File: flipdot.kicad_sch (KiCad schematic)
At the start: 48 parts, among them J1 Conn_01x02_Pin, J2 Conn_01x02_Pin, J3 Conn_01x02_Pin, J4 Conn_01x12_Pin, U5 74HC595

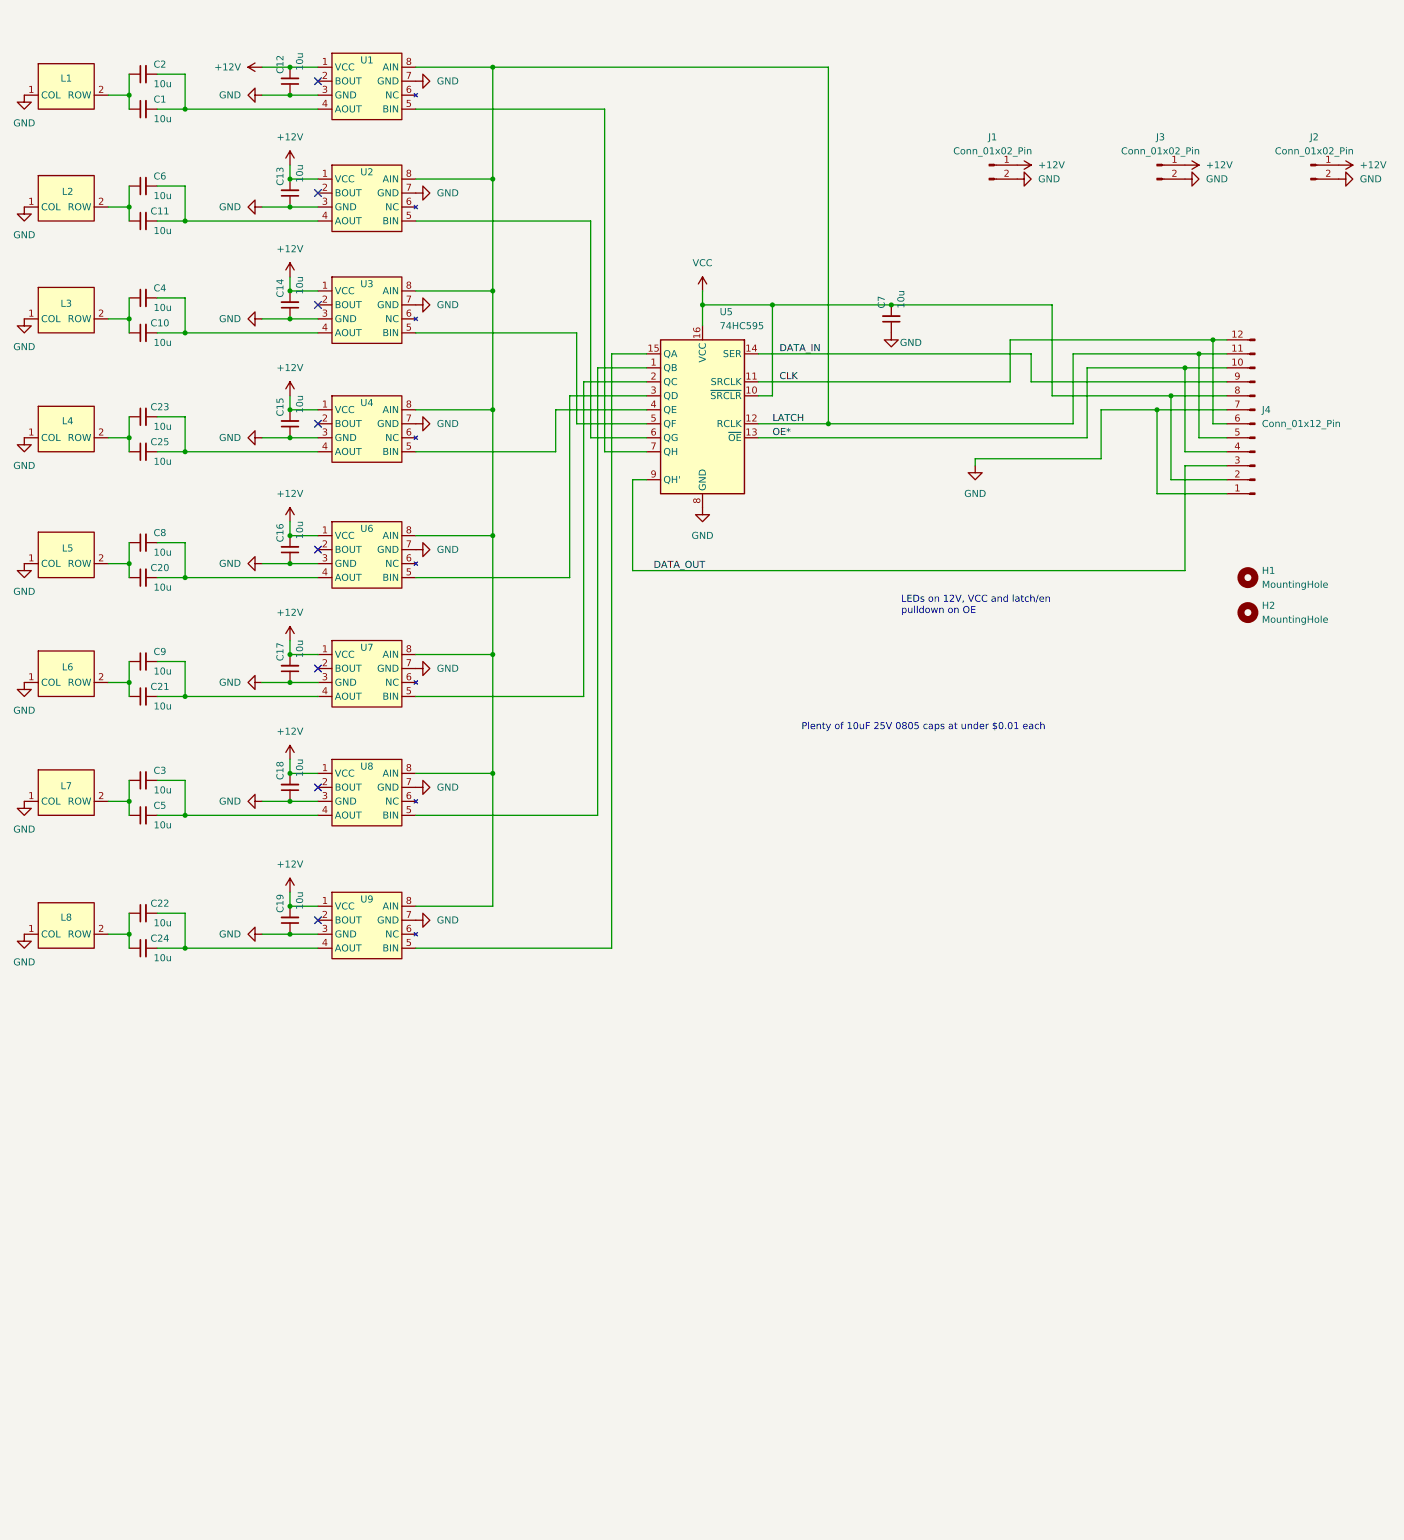
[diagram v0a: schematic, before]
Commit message: split into separate sheets
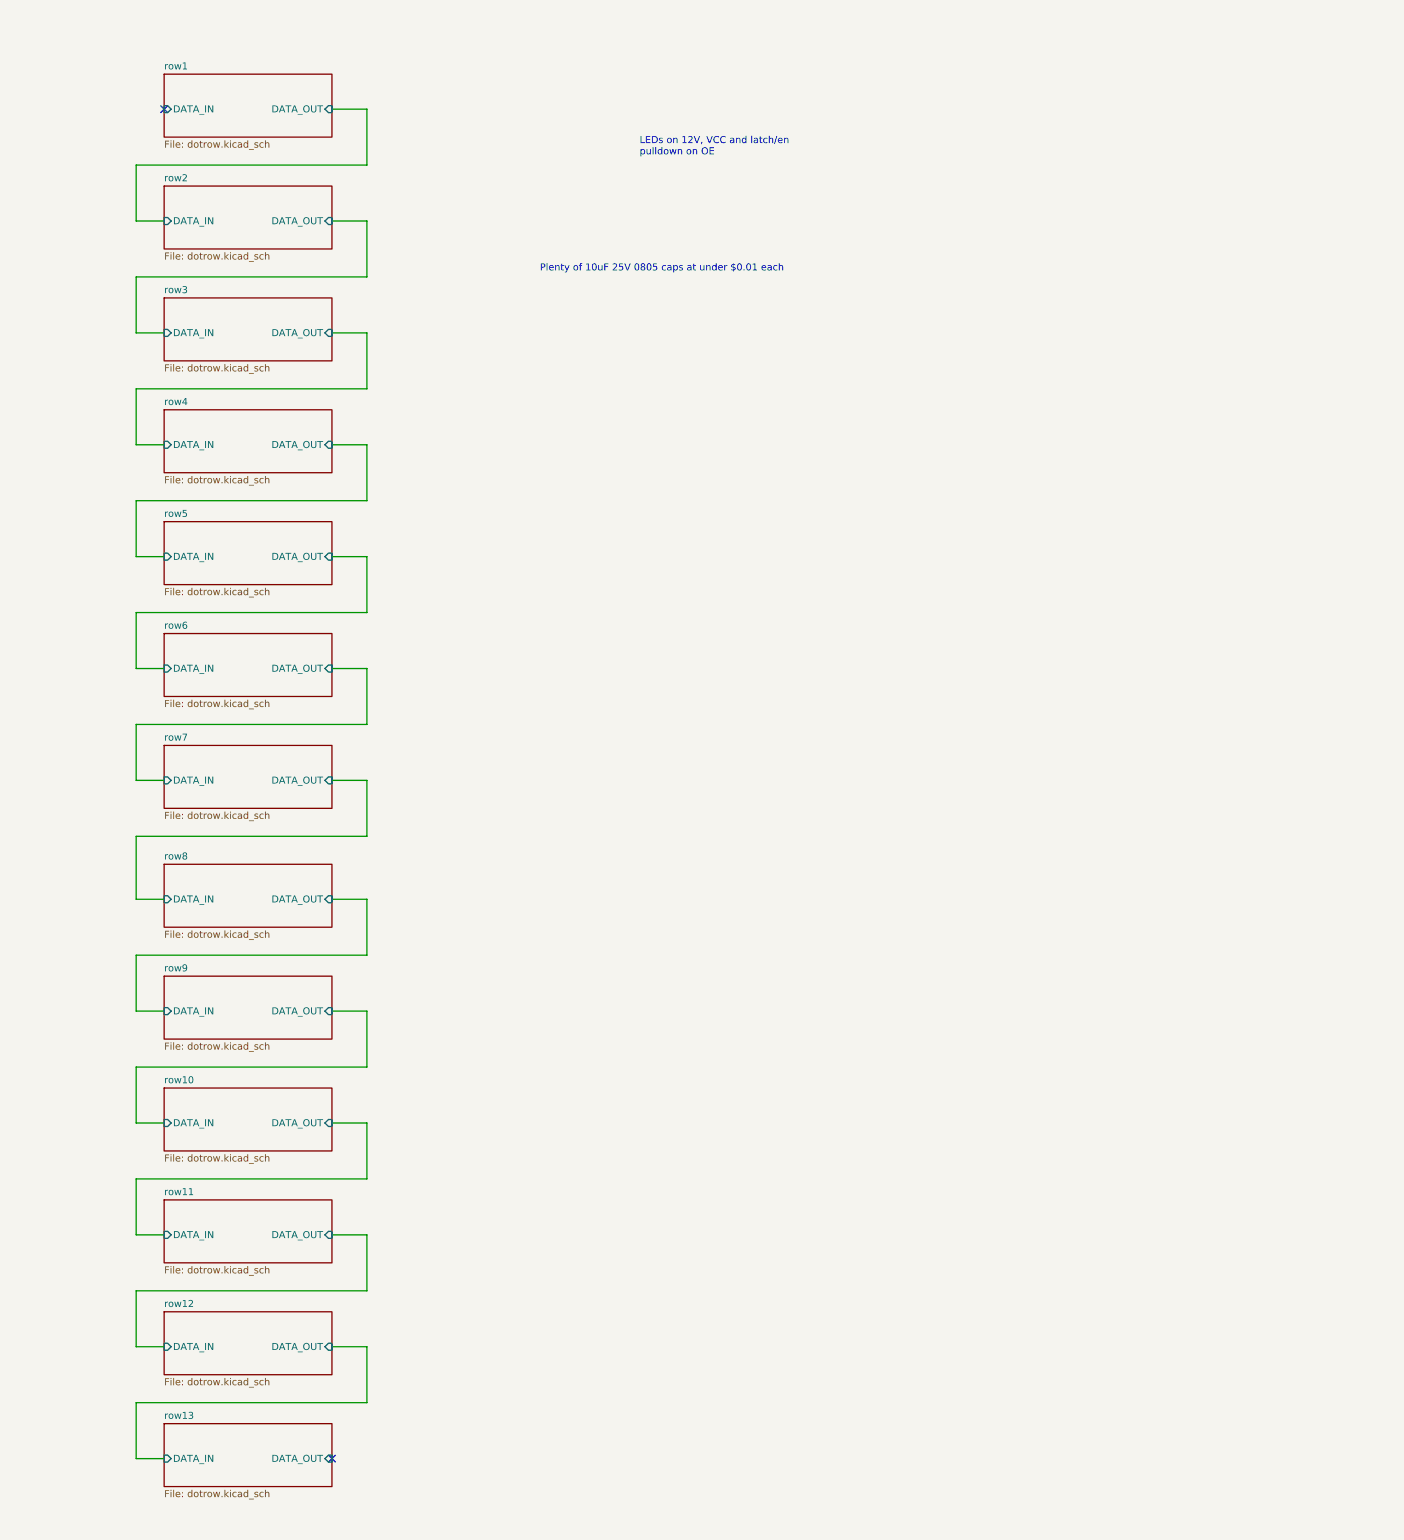
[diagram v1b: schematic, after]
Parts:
- removed C1, C10, C11, C12, C13, C14, C15, C16, C17, C18, C19, C2, C20, C21, C22, C23, C24, C25, C3, C4, C5, C6, C7, C8, C9: 10u, Capacitor_SMD:C_0805_2012Metric, symbol Device:C_Small
- removed H1, H2: MountingHole, MountingHole:MountingHole_3.2mm_M3_DIN965, symbol Mechanical:MountingHole
- removed J1, J2, J3: Conn_01x02_Pin, Connector_JST:JST_VH_B2P-VH_1x02_P3.96mm_Vertical, symbol Connector:Conn_01x02_Pin
- removed J4: Conn_01x12_Pin, Connector_JST:JST_ZH_B6B-ZR_1x06_P1.50mm_Vertical, symbol Connector:Conn_01x12_Pin
- removed L1, L2, L3, L4, L5, L6, L7, L8: ~, Flipdot:Flipdot_single, symbol Flipdot:flipdot_single
- removed U1, U2, U3, U4, U6, U7, U8, U9: ~, Package_SO:SOP-8_3.9x4.9mm_P1.27mm, symbol Flipdot:MX6208
- removed U5: 74HC595, Package_SO:SOP-16_3.9x9.9mm_P1.27mm, symbol 74xx:74HC595
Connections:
- no-connect marks 8 -> 2
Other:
- added sheet row1 (dotrow.kicad_sch)
- added sheet row10 (dotrow.kicad_sch)
- added sheet row11 (dotrow.kicad_sch)
- added sheet row12 (dotrow.kicad_sch)
- added sheet row13 (dotrow.kicad_sch)
- added sheet row2 (dotrow.kicad_sch)
- added sheet row3 (dotrow.kicad_sch)
- added sheet row4 (dotrow.kicad_sch)
- added sheet row5 (dotrow.kicad_sch)
- added sheet row6 (dotrow.kicad_sch)
- added sheet row7 (dotrow.kicad_sch)
- added sheet row8 (dotrow.kicad_sch)
- added sheet row9 (dotrow.kicad_sch)

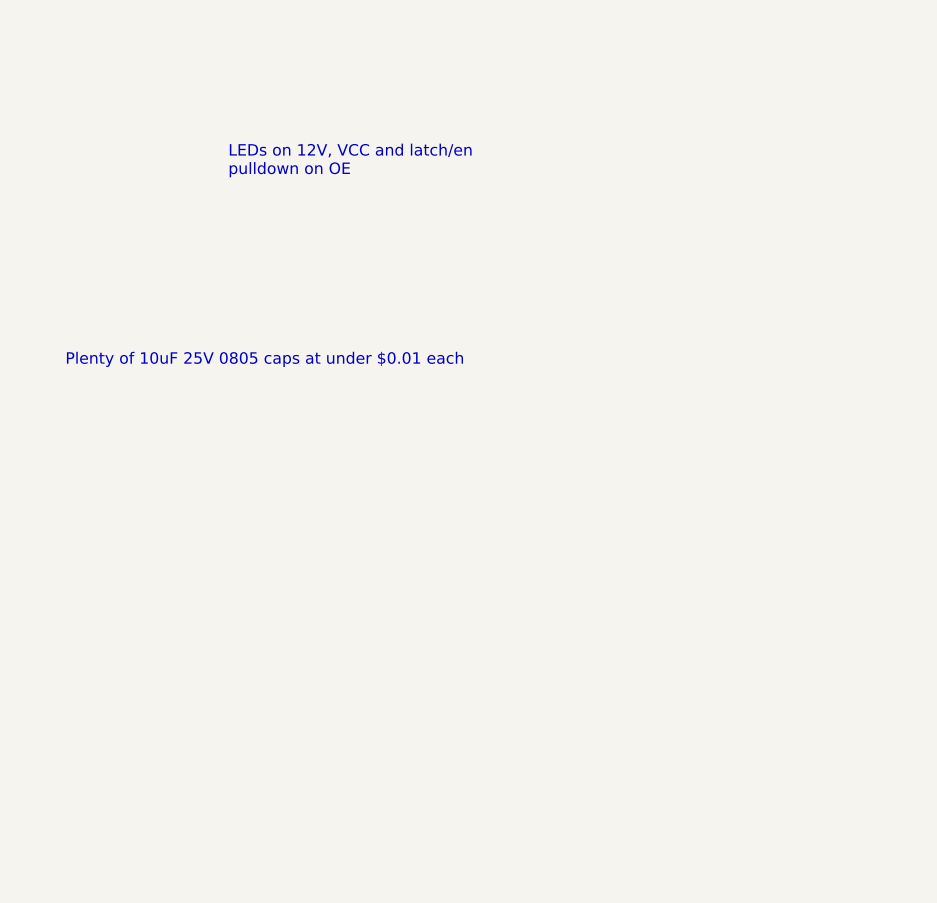
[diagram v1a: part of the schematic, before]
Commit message: add LEDs
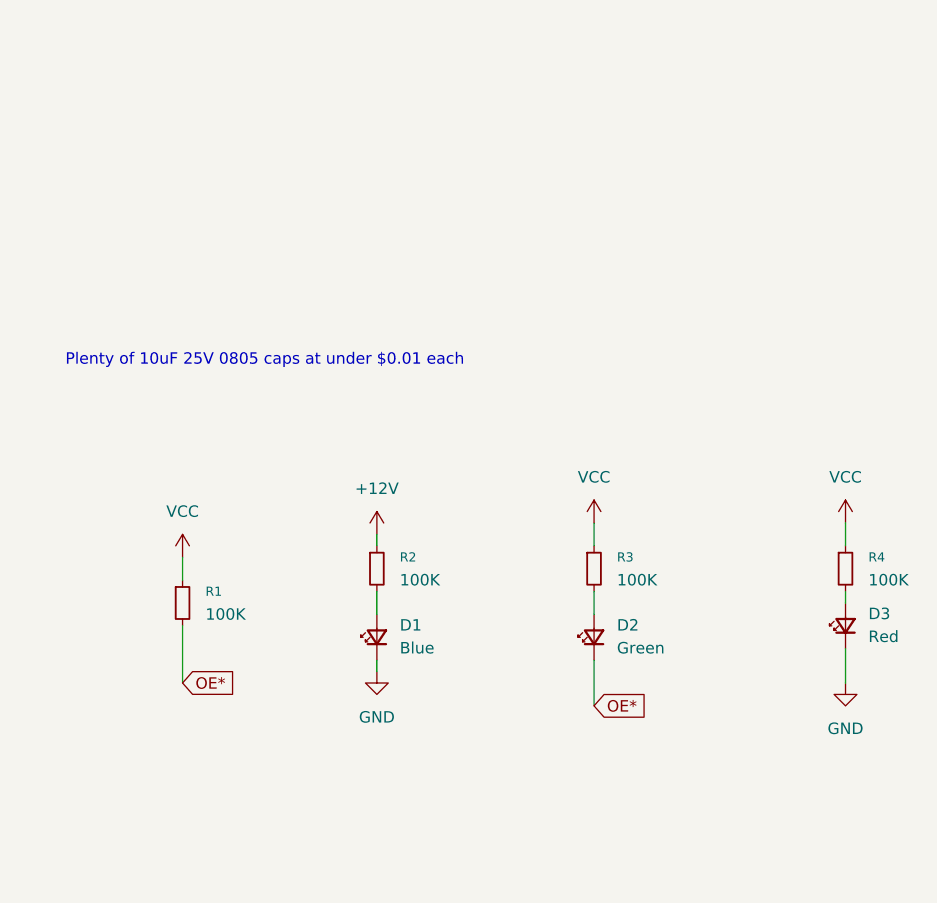
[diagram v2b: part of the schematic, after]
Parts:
- added D1: Blue, LED_SMD:LED_0603_1608Metric, symbol Device:LED_Small
- added D2: Green, LED_SMD:LED_0603_1608Metric, symbol Device:LED_Small
- added D3: Red, LED_SMD:LED_0603_1608Metric, symbol Device:LED_Small
- added R1, R2, R3, R4: 100K, Resistor_SMD:R_0603_1608Metric, symbol Device:R_Small
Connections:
- new net: D1.2 (A), R2.2
- new net: D3.2 (A), R4.2
- new net: D2.2 (A), R3.2
- new net +12V: R2.1
- new net GND: D1.1 (K), D3.1 (K)
- new net OE*: D2.1 (K), R1.2
- new net VCC: R1.1, R3.1, R4.1
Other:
- note removed: "LEDs on 12V, VCC and latch/en pulldown on OE"

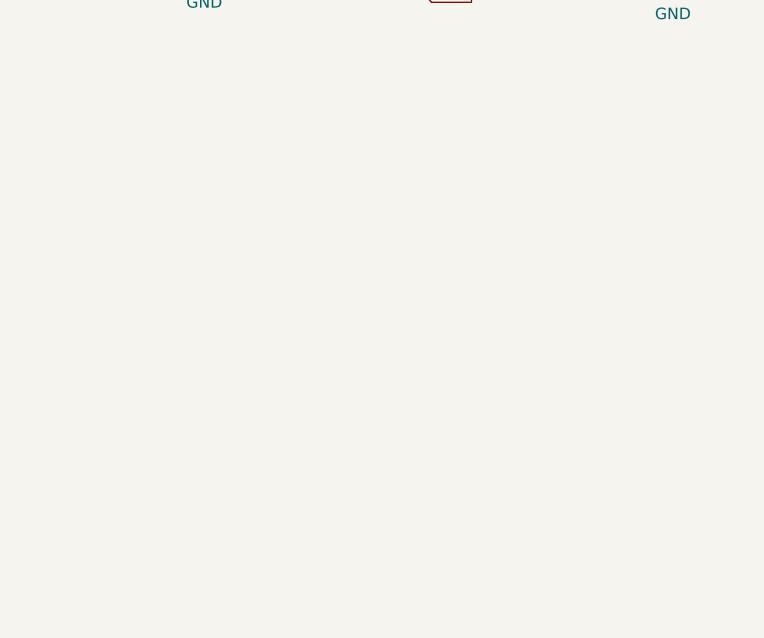
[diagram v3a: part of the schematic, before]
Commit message: add mosfet
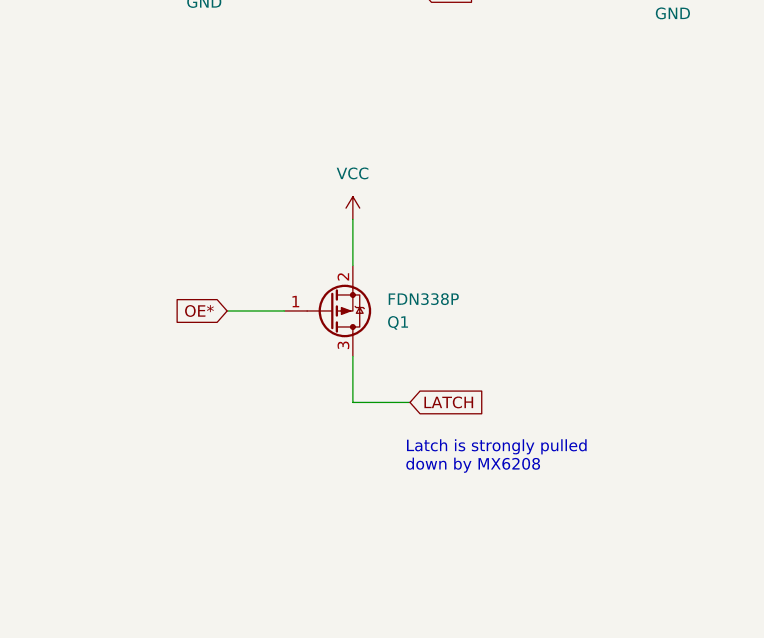
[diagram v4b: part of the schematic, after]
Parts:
- added Q1: FDN338P, Package_TO_SOT_SMD:SOT-23, symbol Transistor_FET:FDN340P
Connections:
- net OE*: now also Q1.1 (G)
- net VCC: now also Q1.2 (S)
- new net LATCH: Q1.3 (D)
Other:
- note added: "Latch is strongly pulled down by MX6208"

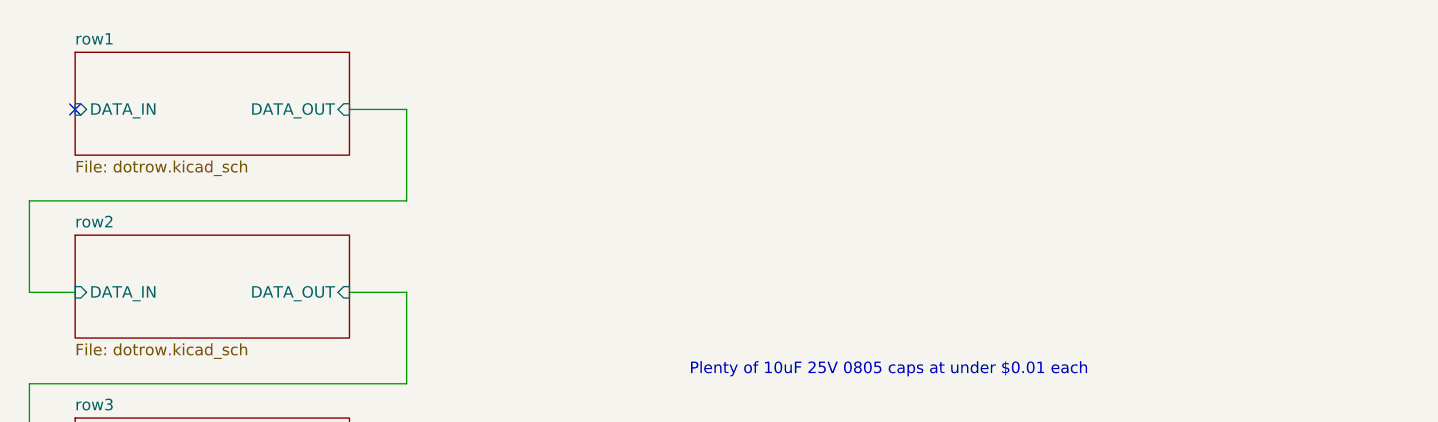
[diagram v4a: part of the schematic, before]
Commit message: replace data connectors with just two 5-pin ZH
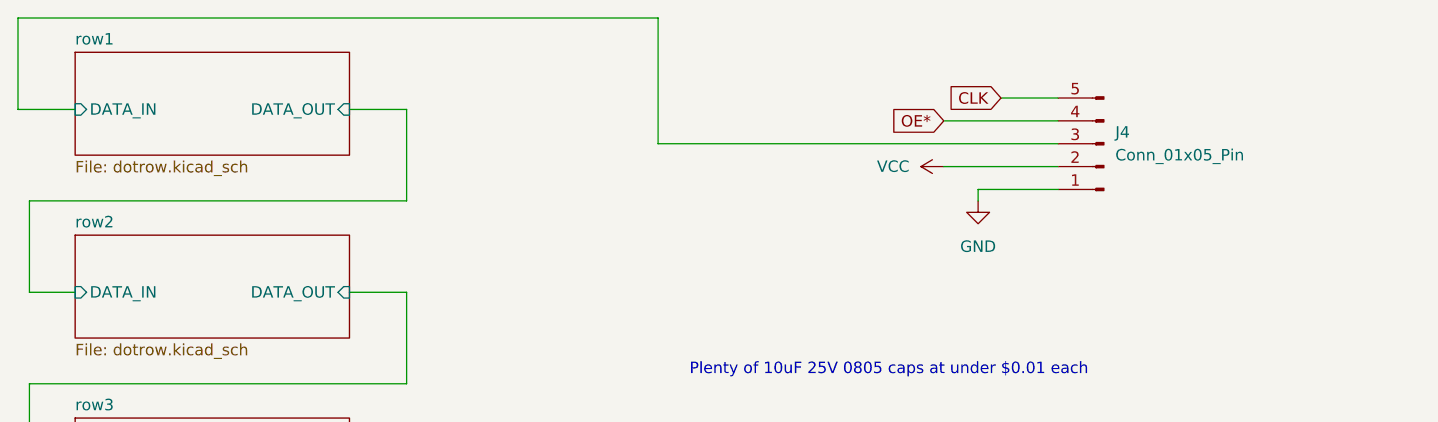
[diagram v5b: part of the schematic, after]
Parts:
- added J4: Conn_01x05_Pin, Connector_JST:JST_ZH_B5B-ZR_1x05_P1.50mm_Vertical, symbol Connector:Conn_01x05_Pin
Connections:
- net GND: now also J4.1 (Pin_1)
- net OE*: now also J4.4 (Pin_4)
- net VCC: now also J4.2 (Pin_2)
- net row1/DATA_IN: now also J4.3 (Pin_3)
- new net CLK: J4.5 (Pin_5)
- no-connect marks 2 -> 1

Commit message: The slow and painful process begins
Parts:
- added J8: Conn_01x05_Pin, Connector_JST:JST_ZH_B5B-ZR_1x05_P1.50mm_Vertical, symbol Connector:Conn_01x05_Pin
- J4: KiLib_Generator (none) -> connector/JST
- Q1: KiLib_Generator (none) -> package/gullwing
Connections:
- net CLK: now also J8.5 (Pin_5)
- net GND: now also J8.1 (Pin_1)
- net OE*: now also J8.4 (Pin_4)
- net VCC: now also J8.2 (Pin_2)
- net row13/DATA_OUT: now also J8.3 (Pin_3)
- no-connect marks 1 -> 0
